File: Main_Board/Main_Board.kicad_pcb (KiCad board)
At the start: 4 copper layers, 120 x 140 mm, 67 parts, among them J1 Conn_01x06, J10 HR-SR04_L_CONN, J11 12V_OUT, J12 BATT_REG_IN, J13 LED_CONN, J14 PD_CONN, J2 Conn_01x06, J3 Conn_01x06, J4 BATT_IN, J5 Conn_02x08_Top_Bottom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

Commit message: Finished Power Planes and layout, started drawing traces [MAIN BOARD]
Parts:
- removed the D3 at (111.8, 50.8)
- added D2: WS2812B, LED_SMD:LED_WS2812B_PLCC4_5.0x5.0mm_P3.2mm, F.Cu at (149.2, 155.5)
- J4: footprint Main_Board:AMASS_XT60-M -> Main_Board:AMASS_XT60PW-M
- J7: footprint Connector_JST:JST_EH_B4B-EH-A_1x04_P2.50mm_Vertical -> Connector_PinSocket_2.54mm:PinSocket_1x04_P2.54mm_Vertical
- J8, R12: moved to B.Cu
- R16, R17: footprint Resistor_SMD:R_0805_2012Metric -> Resistor_SMD:R_0603_1608Metric
- SW2: footprint Main_Board:EG1218 -> Main_Board:EVP-BT2J4A000
- moved R7 238.9 mm to (106.7, 139.7), turned to 90 degrees
- moved R5 216.4 mm to (143.0, 73.9), turned to 180 degrees
- moved D10 213.5 mm to (144.9, 57.1), turned to 90 degrees
- moved R17 208.2 mm to (153.8, 81.2)
- moved D11 206.1 mm to (157.1, 80.9), turned to 180 degrees
- moved C9 204.1 mm to (155.4, 75.8)
- moved R4 198.2 mm to (157.8, 32.8)
- moved C2 195.7 mm to (140.5, 69.8), turned to 270 degrees
- moved J7 195.5 mm to (145.3, 38.6), turned to 90 degrees
- moved L1 190.2 mm to (156.0, 72.9)
- moved R9 187.5 mm to (153.7, 66.8), turned to 270 degrees
- moved R11 186.7 mm to (149.9, 66.8), turned to 270 degrees
- moved R10 186.7 mm to (145.3, 66.8), turned to 270 degrees
- moved C3 184.5 mm to (156.5, 69.3)
- moved R16 184.0 mm to (143.1, 57.0), turned to 90 degrees
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- renumbered D4 to D3, D2 to D4
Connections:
- D3 pad 2: Net-(D3-Pad4) -> Net-(D3-Pad2)
- D3 pad 4: Net-(D4-Pad4) -> Net-(D2-Pad2)
- D4 pad 2: Net-(D2-Pad2) -> Net-(D4-Pad2)
- D4 pad 4: Net-(D2-Pad4) -> Net-(D3-Pad2)
- D5 pad 2: Net-(D4-Pad4) -> Net-(D5-Pad2)
- D5 pad 4: Net-(D5-Pad4) -> Net-(D4-Pad2)
- D6 pad 2: Net-(D5-Pad4) -> Net-(D6-Pad2)
- D6 pad 4: Net-(D6-Pad4) -> Net-(D5-Pad2)
- D7 pad 2: Net-(D6-Pad4) -> Net-(D7-Pad2)
- D7 pad 4: Net-(D7-Pad4) -> Net-(D6-Pad2)
- D8 pad 2: Net-(D7-Pad4) -> Net-(D8-Pad2)
- D8 pad 4: Net-(D8-Pad4) -> Net-(D7-Pad2)
- D9 pad 2: Net-(D8-Pad4) -> Net-(D9-Pad2)
- D9 pad 4: LED_DIN -> Net-(D8-Pad2)
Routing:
- net +3V3: track 0.00 -> 65.3 mm, vias 0 -> 23
- net GND: track 0.00 -> 54.4 mm, vias 0 -> 20
- net Net-(D12-Pad2): track 0.00 -> 18.1 mm, vias 0 -> 2
- net Net-(R5-Pad1): track 0.00 -> 16.3 mm, vias 0 -> 1
- net Net-(U1-Pad12): track 19.9 -> 35.2 mm
- net Net-(U1-Pad11): track 19.9 -> 35.2 mm
- net Net-(U1-Pad10): track 19.9 -> 35.2 mm
- net Net-(R2-Pad1): track 0.00 -> 11.7 mm, vias 0 -> 1
- net HOLD_SW: track 0.00 -> 9.52 mm
- net Net-(R6-Pad1): track 0.00 -> 9.21 mm
- net Net-(C8-Pad2): track 0.00 -> 6.26 mm
- net Net-(C3-Pad1): track 0.00 -> 5.36 mm
- net Net-(R10-Pad2): track 0.00 -> 5.31 mm
- net Net-(C5-Pad2): track 0.00 -> 5.14 mm
- net Net-(R13-Pad2): track 0.00 -> 5.11 mm
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- added copper zone on F.Cu, net +12V
- added copper zone on In1.Cu, net +12V
- added copper zone on F.Cu, net +3V3
- added copper zone on In1.Cu, net +3V3
- added copper zone on F.Cu, net +VDC
- added copper zone on In1.Cu, net +VDC
- added copper zone on F.Cu, net Net-(J11-Pad1)
- added copper zone on F.Cu, net Net-(J4-Pad2)
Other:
- outline, holes or cut-outs redrawn

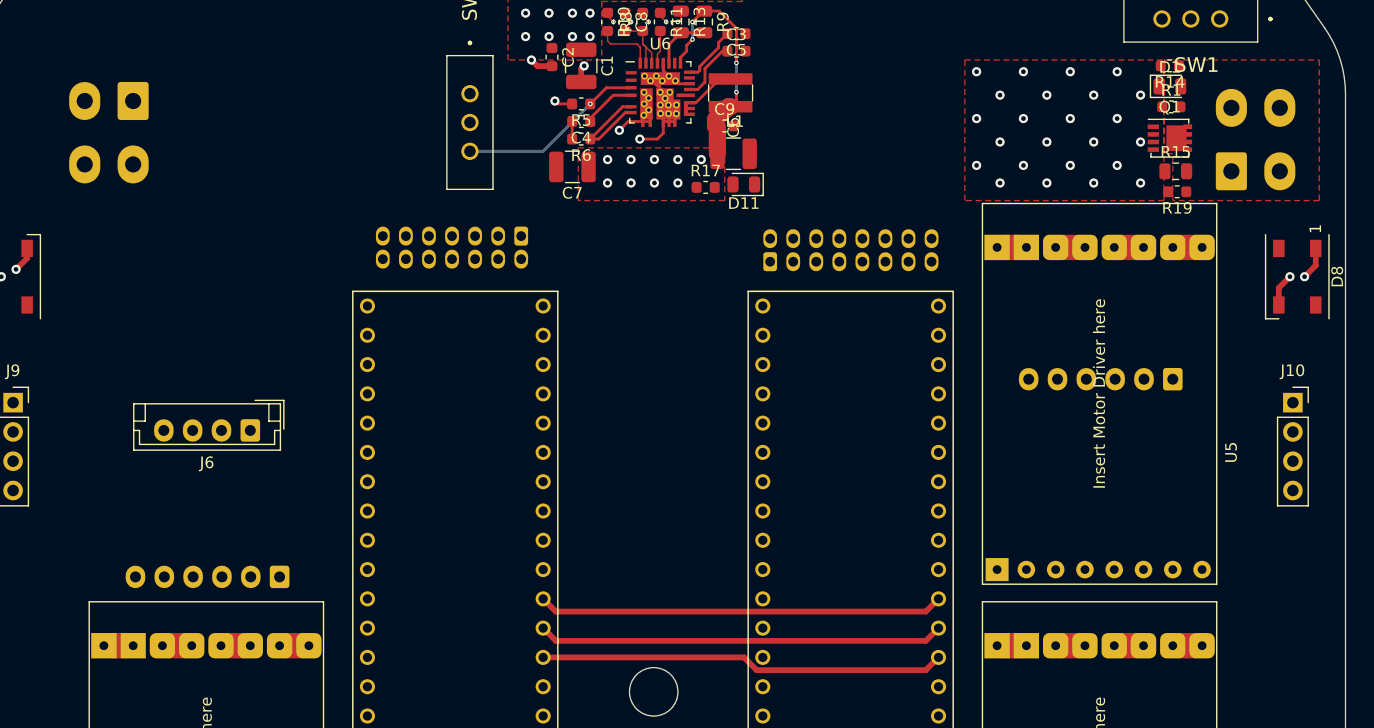
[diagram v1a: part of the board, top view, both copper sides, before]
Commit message: Small changes to 12V connector [MAIN BOARD]
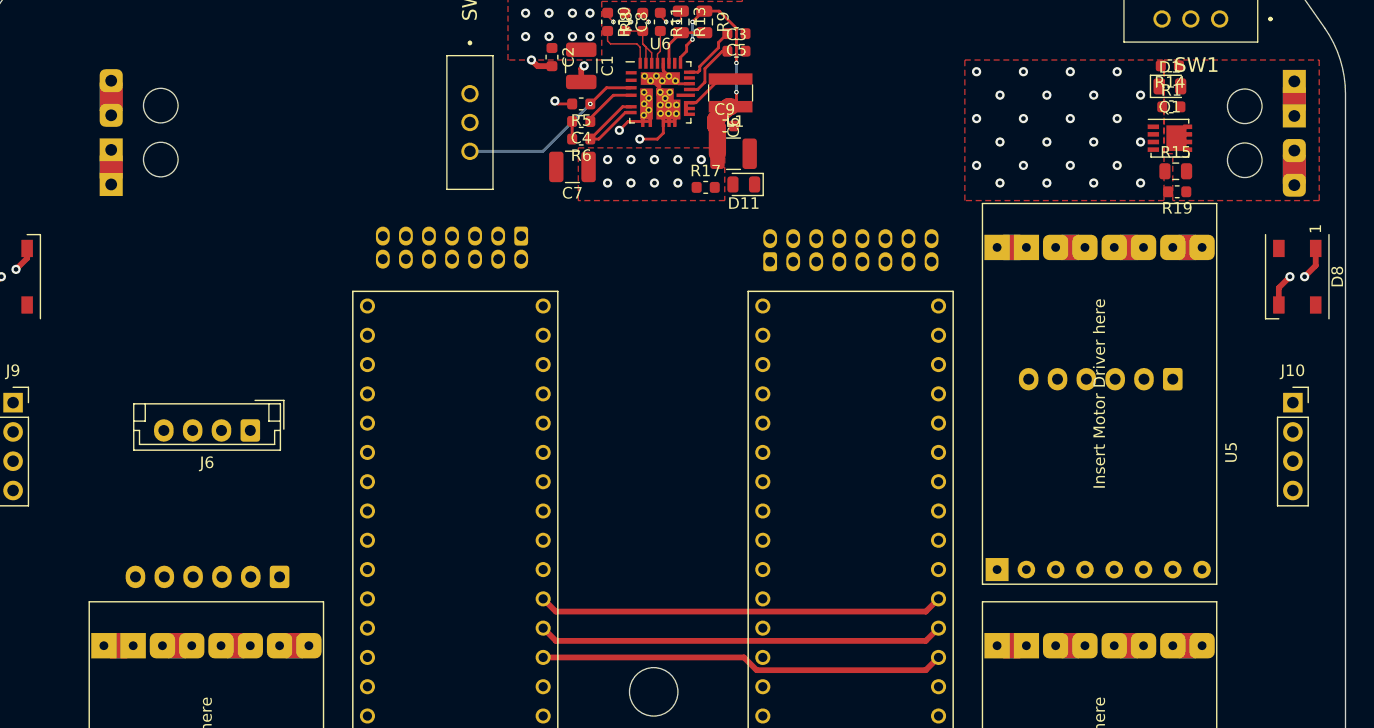
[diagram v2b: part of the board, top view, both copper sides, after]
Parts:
- J11, J12: footprint Connector_Molex:Molex_Mini-Fit_Jr_5566-04A_2x02_P4.20mm_Vertical -> Main_Board:215760-YY04
- moved J11 9.52 mm to (204.9, 72.0), turned to 90 degrees
- moved J12 7.49 mm to (102.2, 80.9), turned to 270 degrees
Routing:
- net GND: vias 20 -> 21
- net +12V: vias 24 -> 23

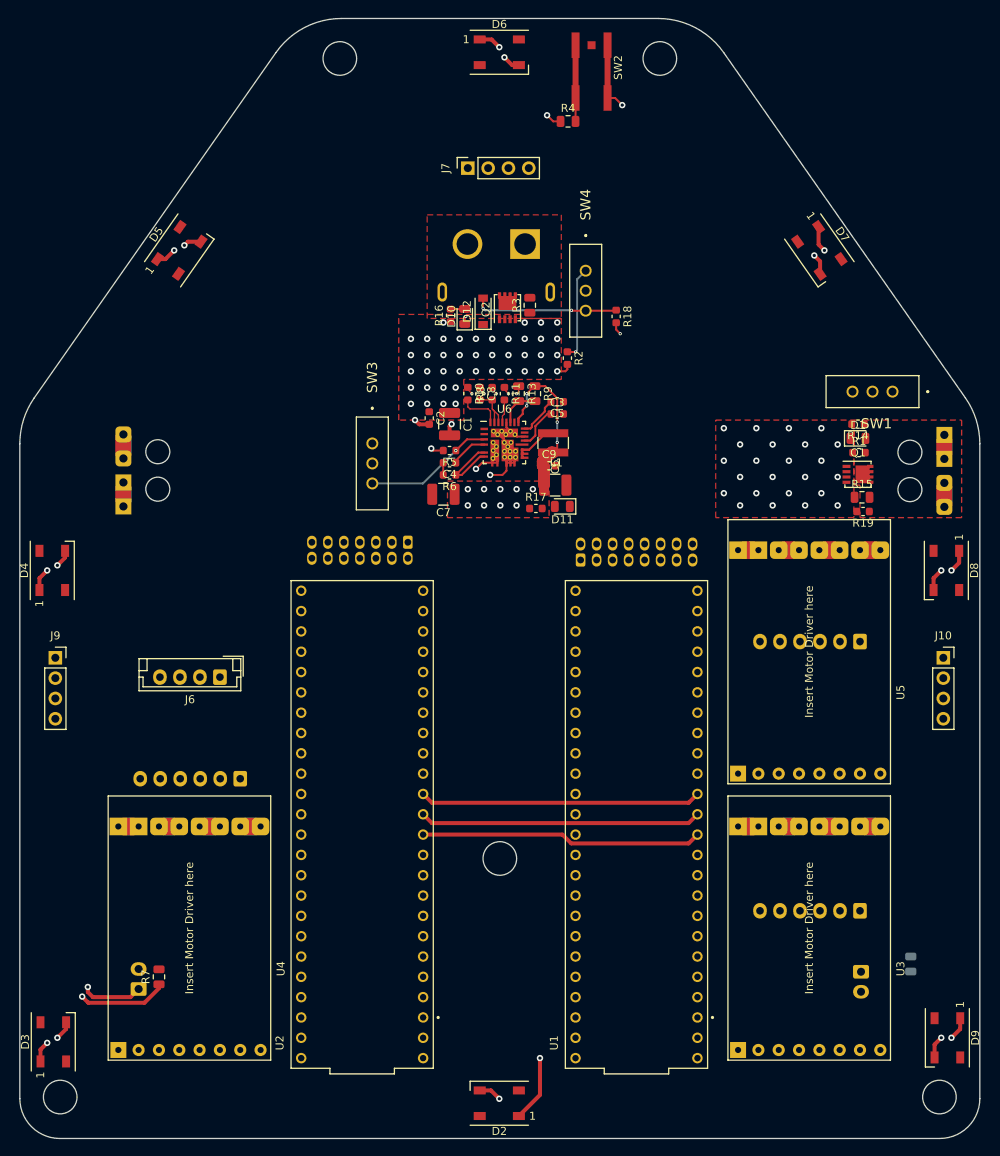
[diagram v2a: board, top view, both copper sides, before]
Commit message: Started actual traces [MAIN BOARD]
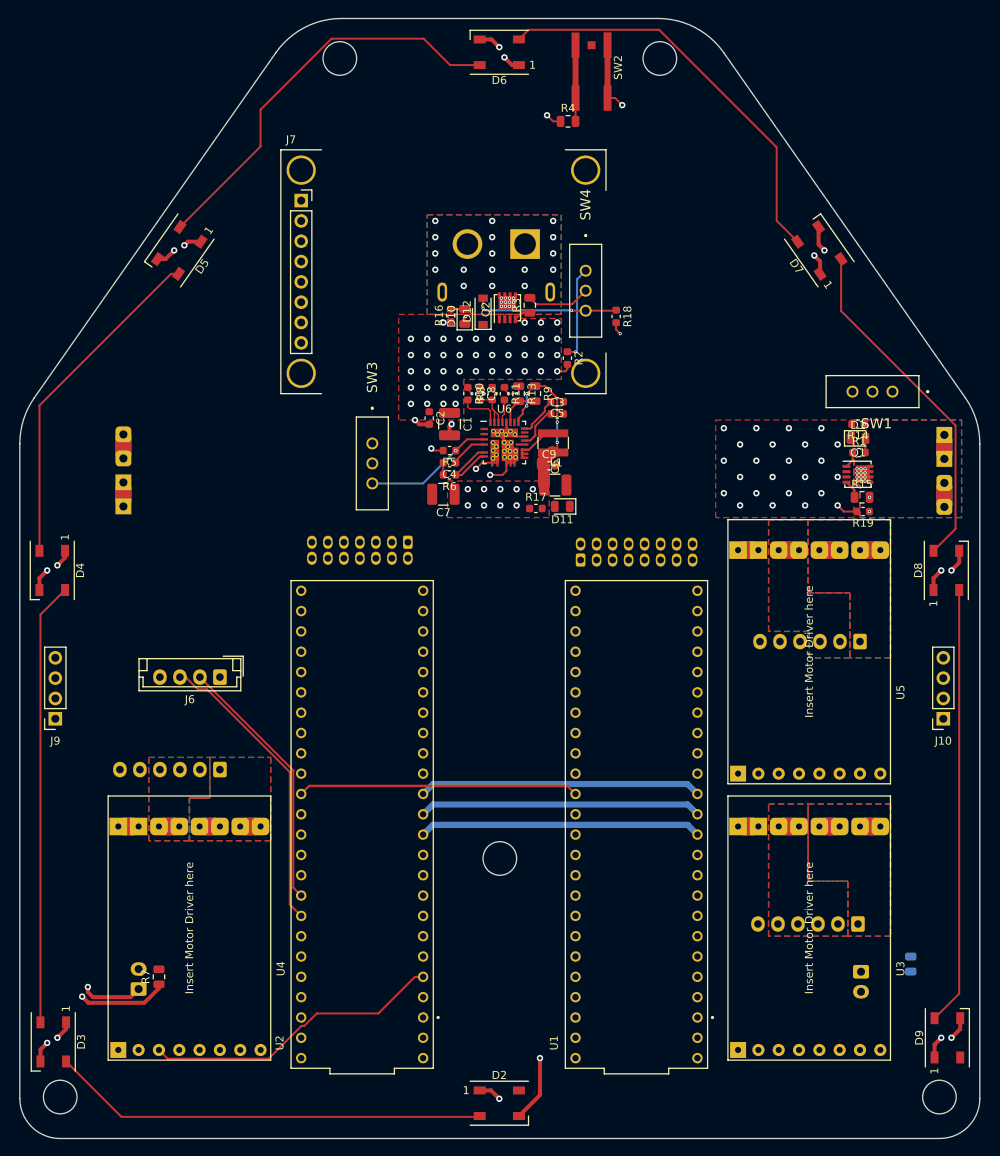
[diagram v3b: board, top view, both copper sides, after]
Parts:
- J7: value OLED_CONN -> Conn_01x08; footprint Connector_PinSocket_2.54mm:PinSocket_1x04_P2.54mm_Vertical -> Connector_PinSocket_2.54mm:PinSocket_1x08_P2.54mm_Vertical
- moved J7 14.2 mm to (144.8, 52.8), turned to 0 degrees
- moved J10 7.62 mm to (204.7, 107.4), turned to 180 degrees
- moved J9 7.62 mm to (93.7, 107.4), turned to 180 degrees
- moved J2 2.79 mm to (114.3, 113.8)
- moved J1 1.67 mm to (194.1, 133.1)
- turned D2 to 0 degrees
- turned D3 to 270 degrees
- turned D4 to 270 degrees
- turned D5 to 235 degrees
- turned D6 to 180 degrees
- turned D7 to 125 degrees
- turned D8 to 90 degrees
- turned D9 to 90 degrees
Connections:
- J7 pad 1: +3V3 -> GND
- J7 pad 2: OLED_SDA -> +3V3
- J7 pad 3: OLED_SCL -> Net-(J7-Pad3)
- J7 pad 4: GND -> Net-(J7-Pad4)
- J8 pad 1: +3V3 -> LIGHT_EN
- J8 pad 10: ~CS -> P3
- J8 pad 11: ~WR -> P0
- J8 pad 12: ~EN -> P1
- J8 pad 13: D -> +3V3
- J8 pad 14: LIGHT_EN -> +3V3
- J8 pad 2: +3V3 -> D
- J8 pad 3: P1 -> ~EN
- J8 pad 4: P0 -> ~WR
- J8 pad 5: P3 -> ~CS
- J8 pad 6: P2 -> GND
- J8 pad 7: P4 -> GND
- J8 pad 8: GND -> P4
- J8 pad 9: GND -> P2
- U1 pad 14: IR1 -> IR12
- U1 pad 15: IR2 -> IR13
- U1 pad 16: IR3 -> IR14
- U1 pad 17: IR4 -> Net-(U1-Pad17)
- U1 pad 18: IR5 -> IR1
- U1 pad 19: IR6 -> IR2
- U1 pad 20: IR7 -> IR3
- U1 pad 21: IR8 -> Net-(U1-Pad21)
- U1 pad 22: IR9 -> IR4
- U1 pad 23: IR10 -> IR5
- U1 pad 24: IR11 -> IR6
- U1 pad 25: IR12 -> Net-(U1-Pad25)
- U1 pad 26: IR13 -> IR7
- U1 pad 27: IR14 -> IR8
- U1 pad 38: Net-(U1-Pad38) -> IR9
- U1 pad 40: Net-(U1-Pad40) -> IR10
- U1 pad 41: Net-(U1-Pad41) -> IR11
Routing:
- net Net-(D3-Pad2): track 0.00 -> 55.3 mm
- net Net-(D8-Pad2): track 0.00 -> 54.8 mm
- net Net-(D2-Pad2): track 0.00 -> 54.6 mm
- net Net-(D6-Pad2): track 0.00 -> 51.7 mm
- net Net-(D5-Pad2): track 0.00 -> 51.3 mm
- net Net-(D7-Pad2): track 0.00 -> 43.5 mm
- net Net-(D4-Pad2): track 0.00 -> 42.4 mm
- net M2_PWM: track 0.00 -> 37.7 mm
- net MAGN_SCL: track 0.00 -> 37.2 mm
- net SCK_MASTER: track 0.00 -> 35.1 mm
- net MAGN_SDA: track 0.00 -> 32.5 mm
- net Net-(R19-Pad1): track 0.00 -> 16.2 mm, vias 0 -> 1
- net Net-(R15-Pad2): track 0.00 -> 13.4 mm, vias 0 -> 1
- net Net-(R3-Pad2): track 0.00 -> 8.02 mm
- net GND: track 54.4 -> 62.4 mm, vias 21 -> 20
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- added copper zone on B.Cu, net M1_A
- added copper zone on F.Cu, net M1_A
- added copper zone on B.Cu, net M1_B
- added copper zone on F.Cu, net M1_B
- added copper zone on B.Cu, net M2_A
- added copper zone on F.Cu, net M2_A
- added copper zone on B.Cu, net M2_B
- added copper zone on F.Cu, net M2_B
- added copper zone on B.Cu, net M3_A
- added copper zone on F.Cu, net M3_A
- added copper zone on B.Cu, net M3_B
- added copper zone on F.Cu, net M3_B
- added copper zone on B.Cu, net Net-(J11-Pad1)
- added copper zone on B.Cu, net Net-(J4-Pad2)

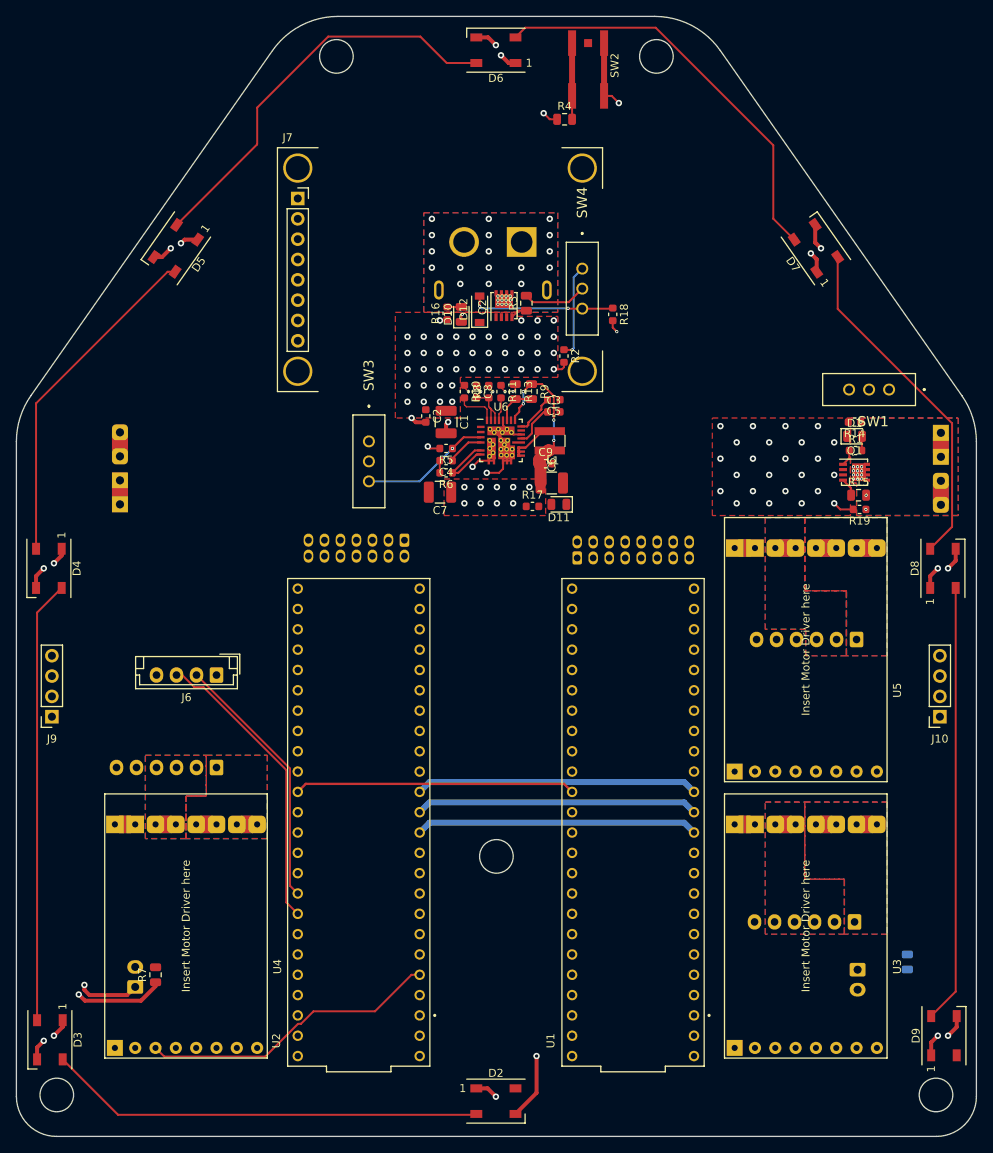
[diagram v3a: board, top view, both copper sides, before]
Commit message: Finished main part traces [MAIN_PCB]
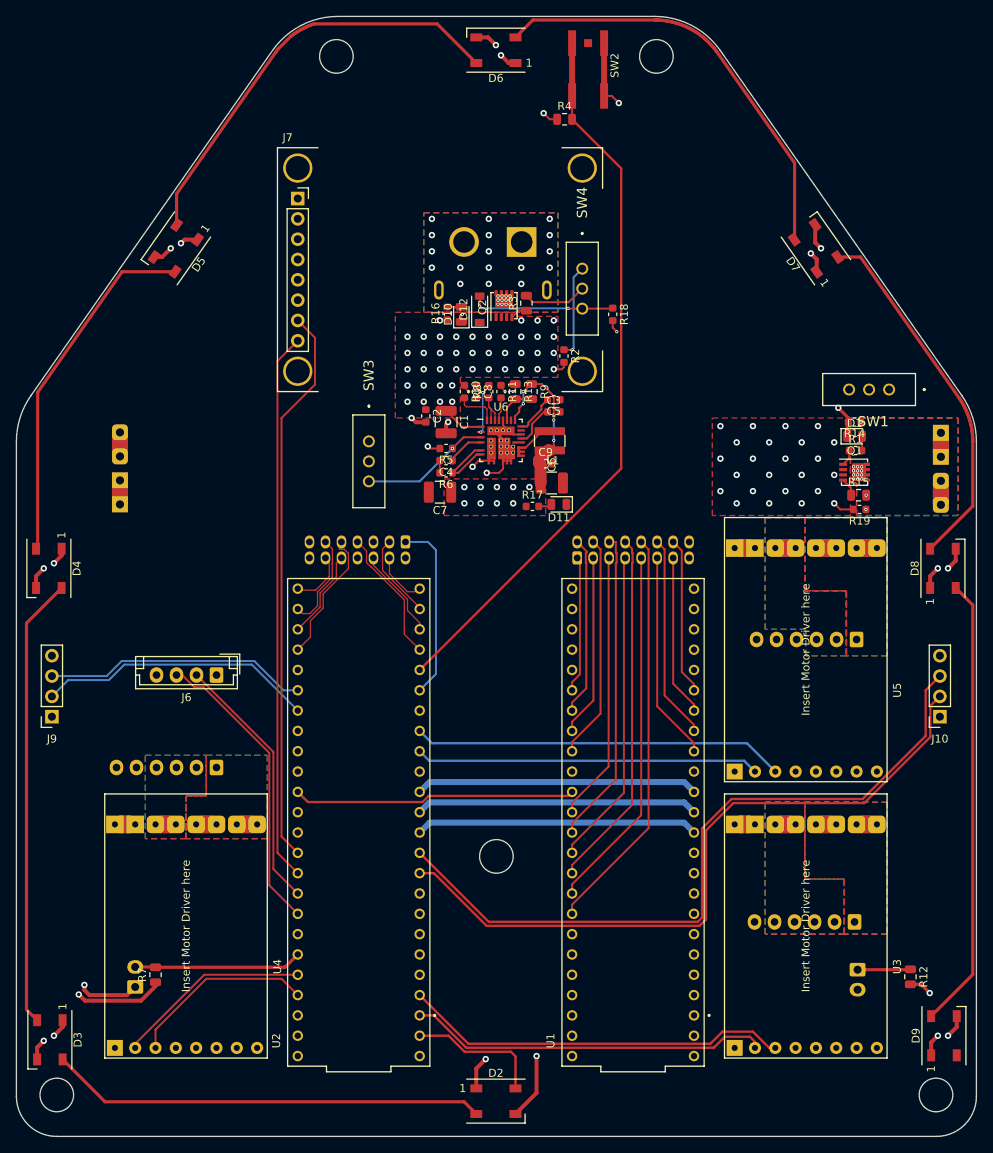
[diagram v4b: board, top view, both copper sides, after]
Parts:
- R12: moved to F.Cu
- moved R12 1.90 mm to (201.0, 140.0), turned to 270 degrees
- moved J8 0.26 mm to (137.9, 85.6)
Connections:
- J5 pad 10: IR9 -> IR10
- J5 pad 11: IR10 -> IR11
- J5 pad 12: IR11 -> IR12
- J5 pad 13: IR12 -> IR13
- J5 pad 14: IR13 -> IR14
- J5 pad 15: IR14 -> +3V3
- J5 pad 16: +3V3 -> GND
- J5 pad 8: GND -> IR8
- J5 pad 9: IR8 -> IR9
- J8 pad 1: LIGHT_EN -> D
- J8 pad 10: P3 -> P2
- J8 pad 11: P0 -> P1
- J8 pad 12: P1 -> P0
- J8 pad 2: D -> LIGHT_EN
- J8 pad 3: ~EN -> ~WR
- J8 pad 4: ~WR -> ~EN
- J8 pad 5: ~CS -> GND
- J8 pad 6: GND -> ~CS
- J8 pad 7: GND -> P4
- J8 pad 8: P4 -> GND
- J8 pad 9: P2 -> P3
- U1 pad 14: IR12 -> IR5
- U1 pad 15: IR13 -> IR6
- U1 pad 16: IR14 -> IR7
- U1 pad 17: Net-(U1-Pad17) -> IR8
- U1 pad 18: IR1 -> IR9
- U1 pad 19: IR2 -> IR10
- U1 pad 20: IR3 -> Net-(U1-Pad20)
- U1 pad 22: IR4 -> Net-(U1-Pad22)
- U1 pad 23: IR5 -> Net-(U1-Pad23)
- U1 pad 24: IR6 -> IR11
- U1 pad 25: Net-(U1-Pad25) -> IR12
- U1 pad 26: IR7 -> IR13
- U1 pad 27: IR8 -> IR14
- U1 pad 38: IR9 -> IR1
- U1 pad 39: Net-(U1-Pad39) -> IR2
- U1 pad 40: IR10 -> IR3
- U1 pad 41: IR11 -> IR4
- U2 pad 0: ~WR -> LED_DIN
- U2 pad 1: ~CS -> M1_DIR
- U2 pad 14: D -> Net-(U2-Pad14)
- U2 pad 15: HOLD_SW -> Net-(U2-Pad15)
- U2 pad 20: PD_OUT -> Net-(U2-Pad20)
- U2 pad 21: Net-(U2-Pad21) -> PD_OUT
- U2 pad 22: Net-(U2-Pad22) -> M2_DIR
- U2 pad 23: Net-(U2-Pad23) -> M2_PWM
- U2 pad 24: Net-(U2-Pad24) -> M3_DIR
- U2 pad 25: Net-(U2-Pad25) -> M3_PWM
- U2 pad 27: Net-(U2-Pad27) -> D
- U2 pad 28: P0 -> HOLD_SW
- U2 pad 29: P1 -> P4
- U2 pad 3: M2_PWM -> Net-(U2-Pad3)
- U2 pad 30: M1_DIR -> ~CS
- U2 pad 31: M2_DIR -> ~WR
- U2 pad 32: M3_DIR -> ~EN
- U2 pad 33: LIGHT_EN -> P0
- U2 pad 34: P2 -> P1
- U2 pad 35: P3 -> P2
- U2 pad 36: P4 -> P3
- U2 pad 37: ~EN -> Net-(U2-Pad37)
- U2 pad 38: Net-(U2-Pad38) -> ECHO_R
- U2 pad 39: Net-(U2-Pad39) -> TRIG_R
- U2 pad 4: M3_PWM -> Net-(U2-Pad4)
- U2 pad 5: TRIG_L -> Net-(U2-Pad5)
- U2 pad 6: ECHO_L -> Net-(U2-Pad6)
- U2 pad 7: TRIG_R -> Net-(U2-Pad7)
- U2 pad 8: ECHO_R -> TRIG_L
- U2 pad 9: LED_DIN -> ECHO_L
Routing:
- net ECHO_L: track 0.00 -> 91.2 mm
- net TRIG_L: track 0.00 -> 88.4 mm
- net HOLD_SW: track 9.52 -> 91.4 mm
- net OLED_SCL: track 0.00 -> 70.0 mm
- net OLED_SDA: track 0.00 -> 68.7 mm
- net IR10: track 0.00 -> 50.8 mm
- net M1_PWM: track 0.00 -> 48.4 mm
- net M3_PWM: track 0.00 -> 46.6 mm
- net IR9: track 0.00 -> 45.5 mm
- net M1_DIR: track 0.00 -> 45.2 mm
- net IR8: track 0.00 -> 44.9 mm
- net M3_DIR: track 0.00 -> 43.0 mm
- net IR7: track 0.00 -> 39.6 mm
- net IR6: track 0.00 -> 39.5 mm
- net TRIG_R: track 0.00 -> 34.8 mm
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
